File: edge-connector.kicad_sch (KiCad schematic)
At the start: 2 parts, among them J5 SFF-TA-1002-4C+

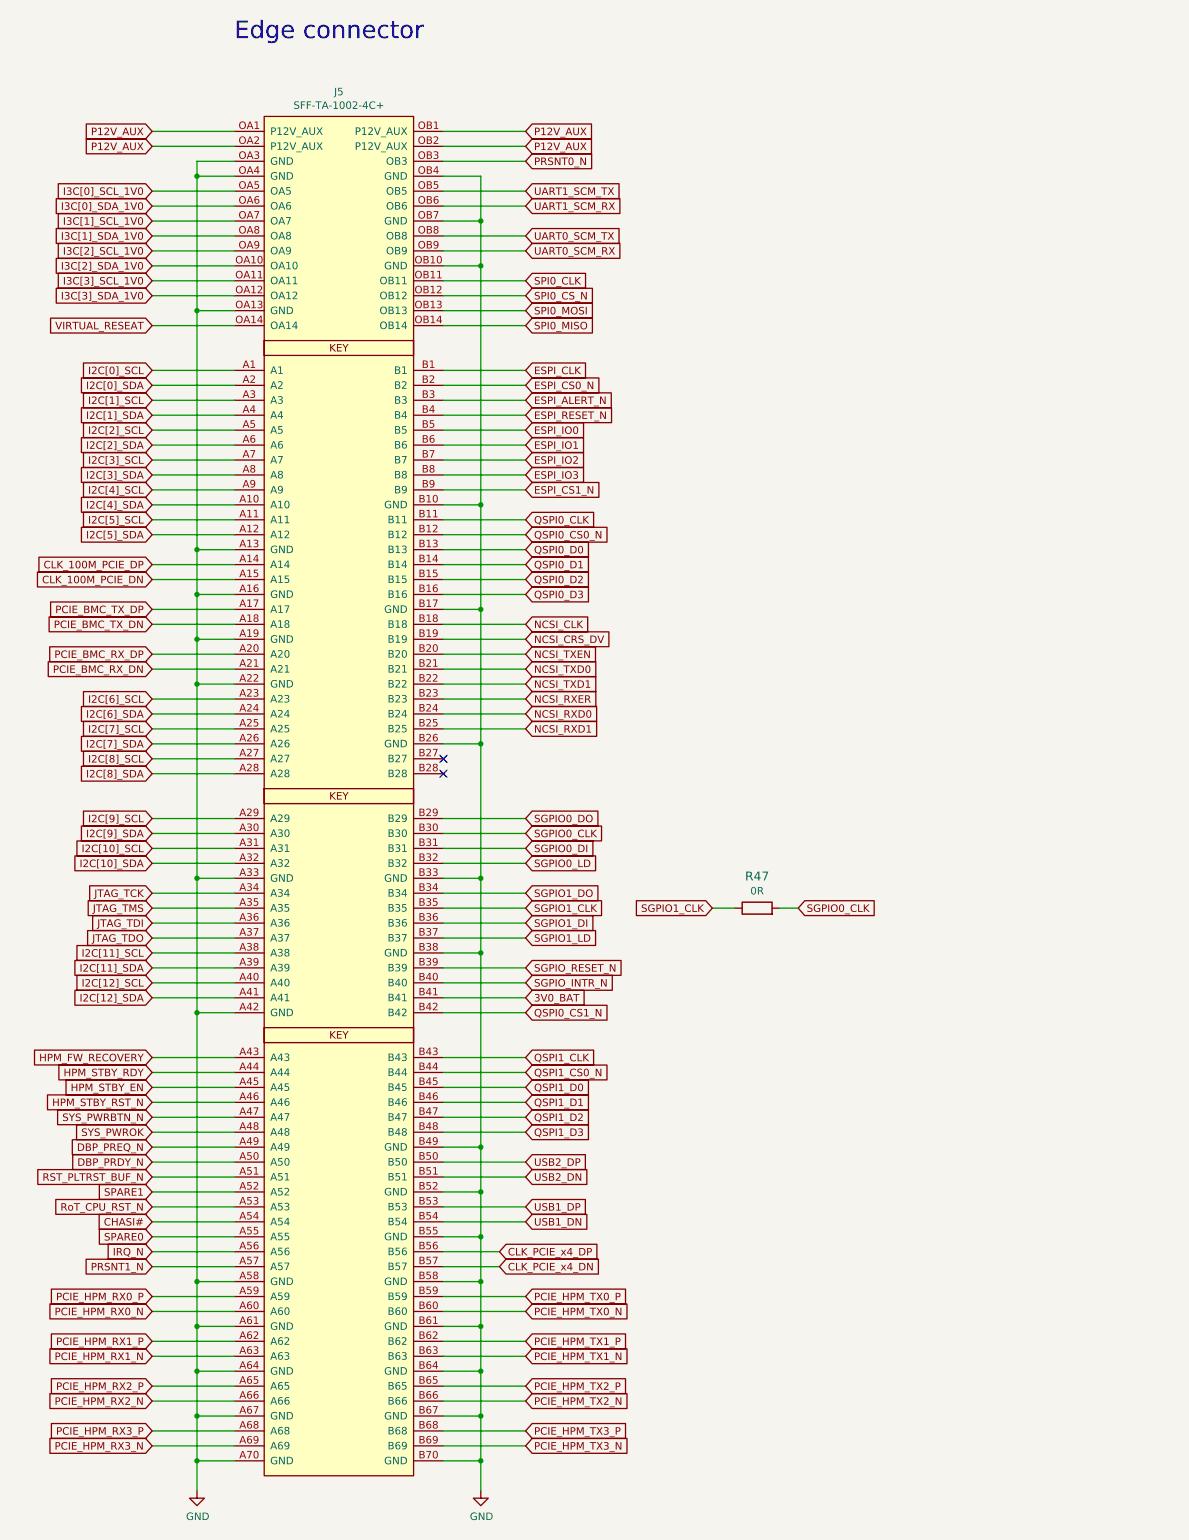
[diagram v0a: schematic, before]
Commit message: [#61392] Convert project to KiCad 7
[#61392] Run globlib

[#61392] Allign components to the grid

[#61392] Update oshw and antmicro logo

[#61392] Standarize ethernet sheet

[#61392] Standarize pcie-conn sheet

[#61392] Standarize rot sheet

[#61392] Standarize edge-connector sheet

[#61392] WIP:Standarize interfaces sheet

[#61392] WIP: Route interfaces sheet

[#61392] Finish standarizing interfaces sheet

[#61392] Update interfaces sheet with fixed 2N7002

[#61392] WIP:Standarize ddr3 sheet

[#61392] Standarize ddr3 sheet

[#61392] Standarize power-supply sheet

[#61392] Standarize fpga power-supply sheet

[#61392] Remove TODO comments from power-banks sheet

[#61392] Standarize fpga-banks sheet

[#61392] Ignore Input pins not driven ERC

[#61392] Clear off grid ERCs

[#61392] Exclude ERC DDR3_VTT_EN NC

[#61392] Bump rev to 1.2.1

[#61392] Bump PCB rev to 1.2.1
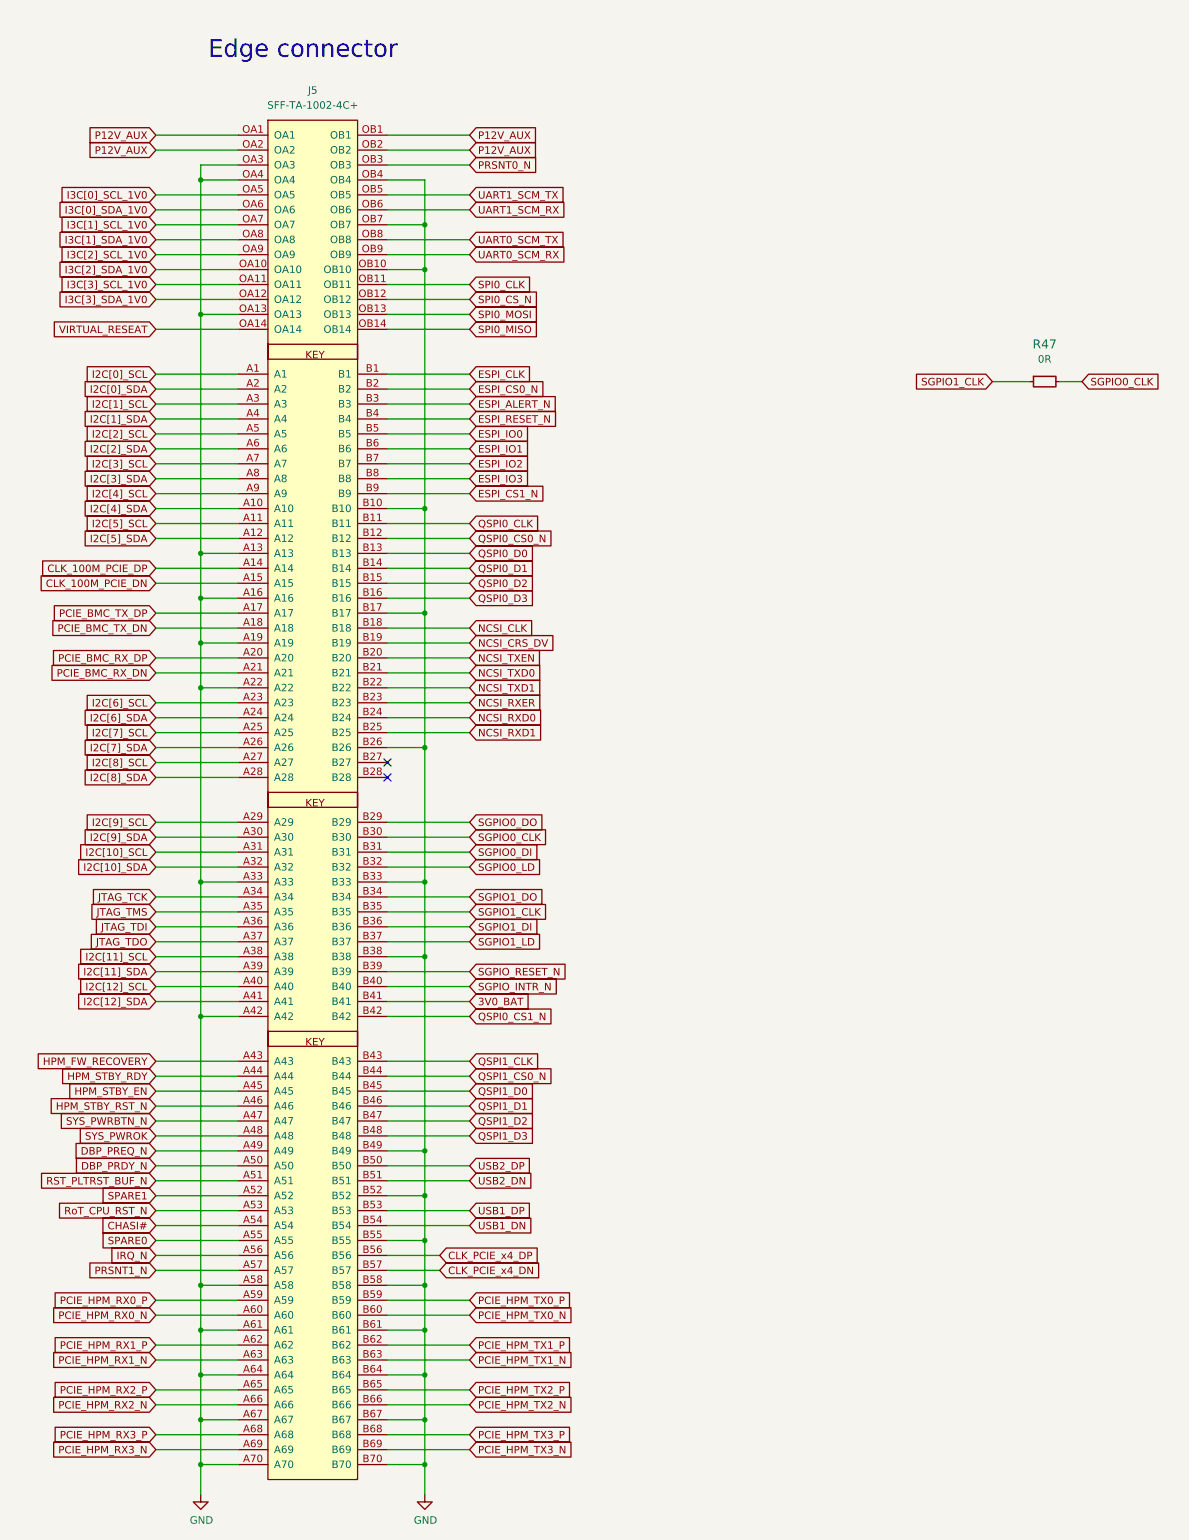
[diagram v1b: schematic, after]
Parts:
- J5: footprint ecp5-dc-scm-footprints:SFF-TA-1002-4C+ -> antmicro-footprints:SFF-TA-1002-4C+; symbol ecp5-dc-scm:SFF-TA-1002-4C+ -> antmicroPciConnectors:SFF-TA-1002-4C+; Author (none) -> Antmicro; License (none) -> Apache-2.0; MPN (none) -> SFF-TA-1002-4C+; Manufacturer (none) -> Amphenol
- R47: footprint ecp5-dc-scm-footprints:0402-res -> antmicro-footprints:R_0402_1005Metric; symbol ecp5-dc-scm:R_0R_0402 -> antmicroResistors0402:R_0R_0402; Author (none) -> Antmicro; Current (none) -> 1A; License (none) -> Apache-2.0; Manufacturer PANASONIC -> Panasonic; Public (none) -> False
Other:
- moved on the sheet: J5, R47

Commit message: [#61392] Import changes to the PCB
[#61392] Fix D2 orientation

[#61392] Fix J2 J1 D6 orientation

[#61392] WIP: PCB Fix caps orienations

[#61392] PCB Fix caps orienations

[#61392] Fix missalligned edge cuts

[#61392] Sync Sch with PCB

[#61392] Fix silk clipped by edge cuts

[#61392] Ignore TP no courtyard drc

[#61392] Update C_0603 footprints

[#61392] Update R_0402 footprints

[#61392] Update Sot-23 footprints

[#61392] Update QFN and IHLP footprints

[#61392] Update remaining footprints

[#61392] Change minimal text height to 0.7mm

[#61392] Clear remaining Silk DRCs

[#61392] Update TPS51200DRCT symbol

[#61392] Update 9774040151

[#61392] Update W25Q32JVS

[#61392] Update ECS-3225MVQ-1000CN-TR

[#61392] Clean ERC

[#61392] Remove obsolete files

[#61392] Synhronize components with library

[#61392] Remove globlib leftovers

[#61392] Synchronize components with libraries (WiP)

[#61392] Clean ERC and DRC

[#61392] Set J5 to DNP

[#61392] Add PCB SHA string, update layer names

[#61392] Update assets

[#62567] Add stackup.csv

[#62567] Input elecric constants for the board stackup

[#62567] Update stackup.csv
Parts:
- J5: DNP (none) -> DNP
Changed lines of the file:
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@@
   (title_block
     (title "ECP5 - Datacenter Secure Control Module (DC-SCM)")
-    (date "2024-07-01")
+    (date "2024-07-15")
     (rev "1.2.1")
   )
@@
       (effects (font (size 1.27 1.27) (thickness 0.15)) (justify left bottom) hide)
     )
+    (property "DNP" "DNP" (at 182.88 39.37 0)
+      (effects (font (size 1.27 1.27)) hide)
+    )
     (pin "A1")
